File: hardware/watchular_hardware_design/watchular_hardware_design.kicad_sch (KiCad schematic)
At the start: 23 parts, among them Q1 BC817, U1 ESP32-C3FH4, U2 W25Q16JVSSIQ

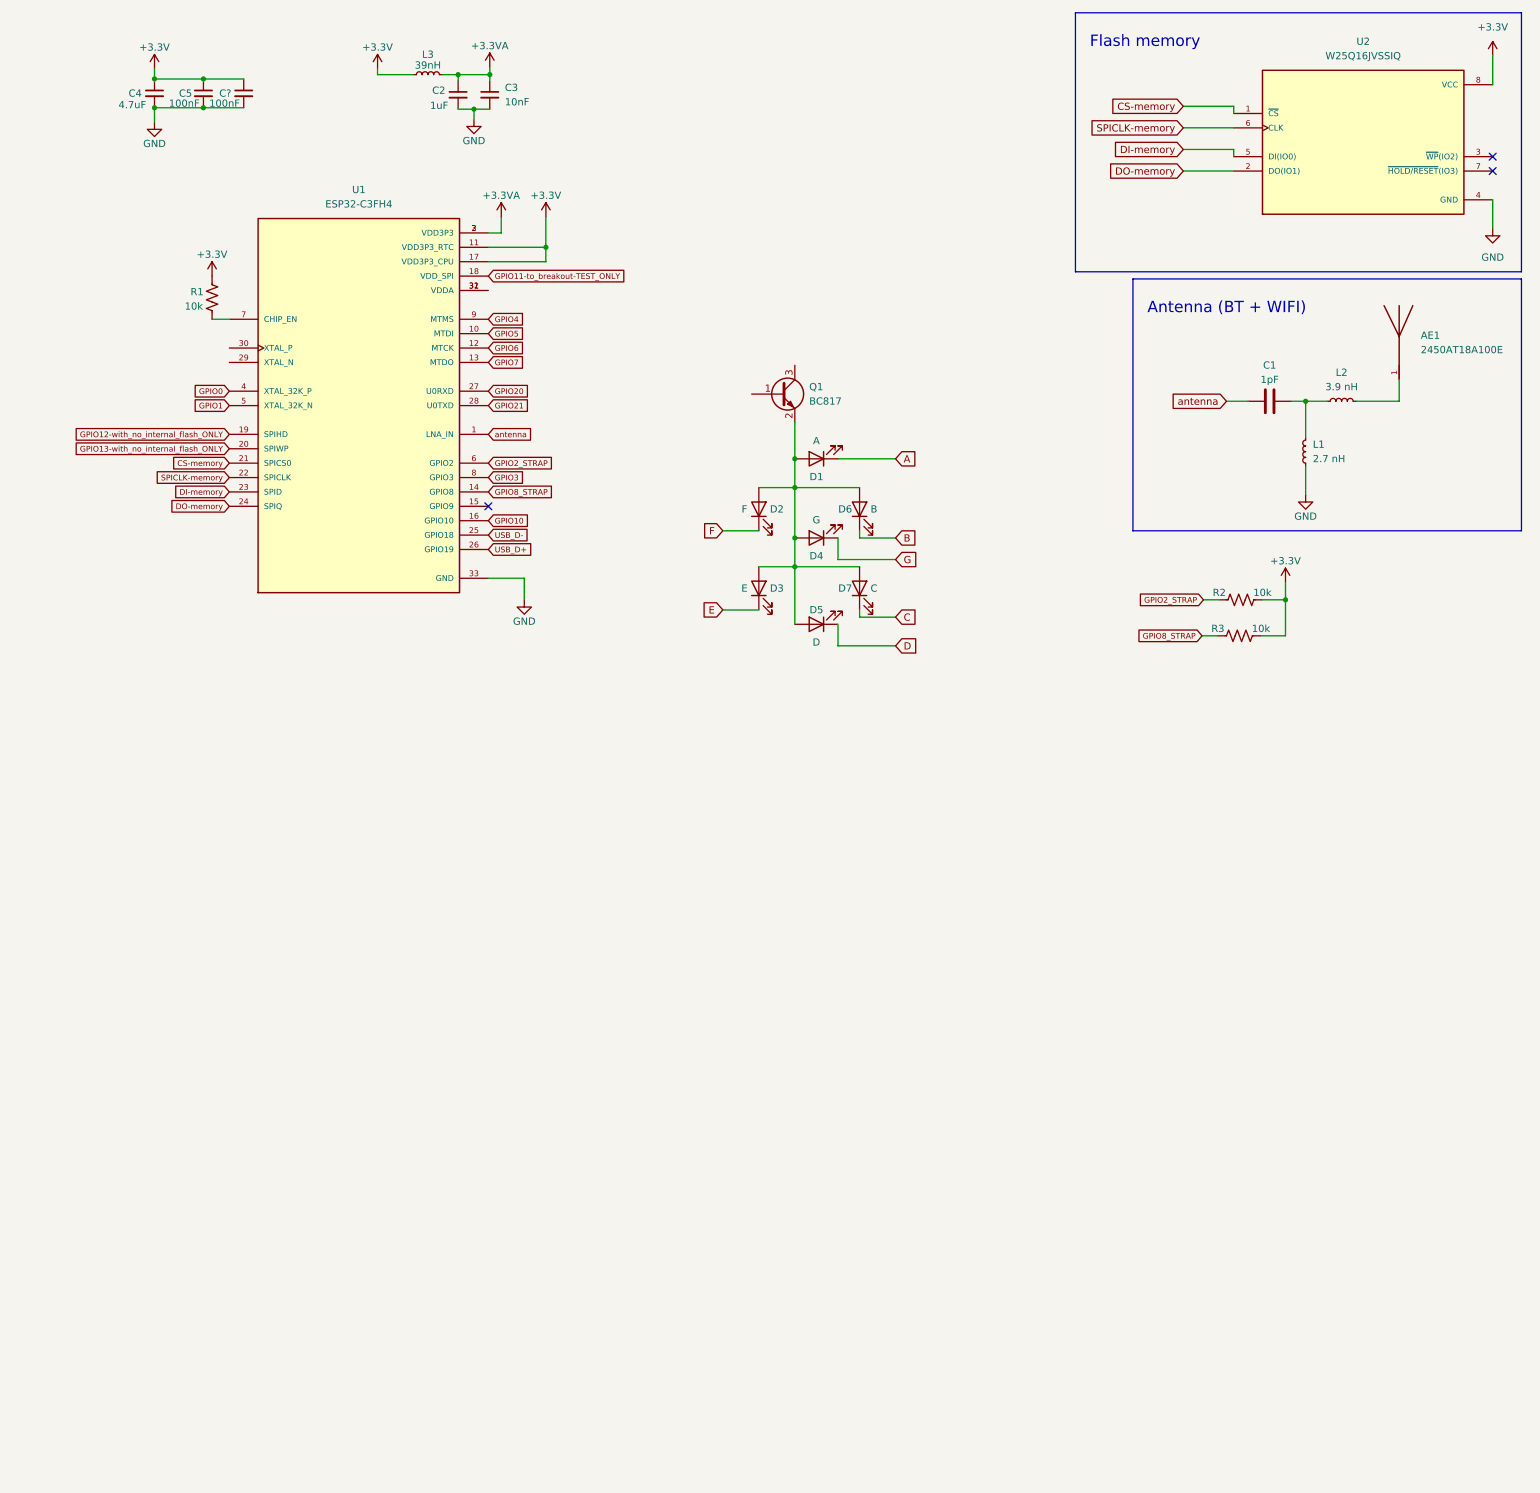
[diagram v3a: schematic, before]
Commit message: Finished the boiler plate for ESP32C3.
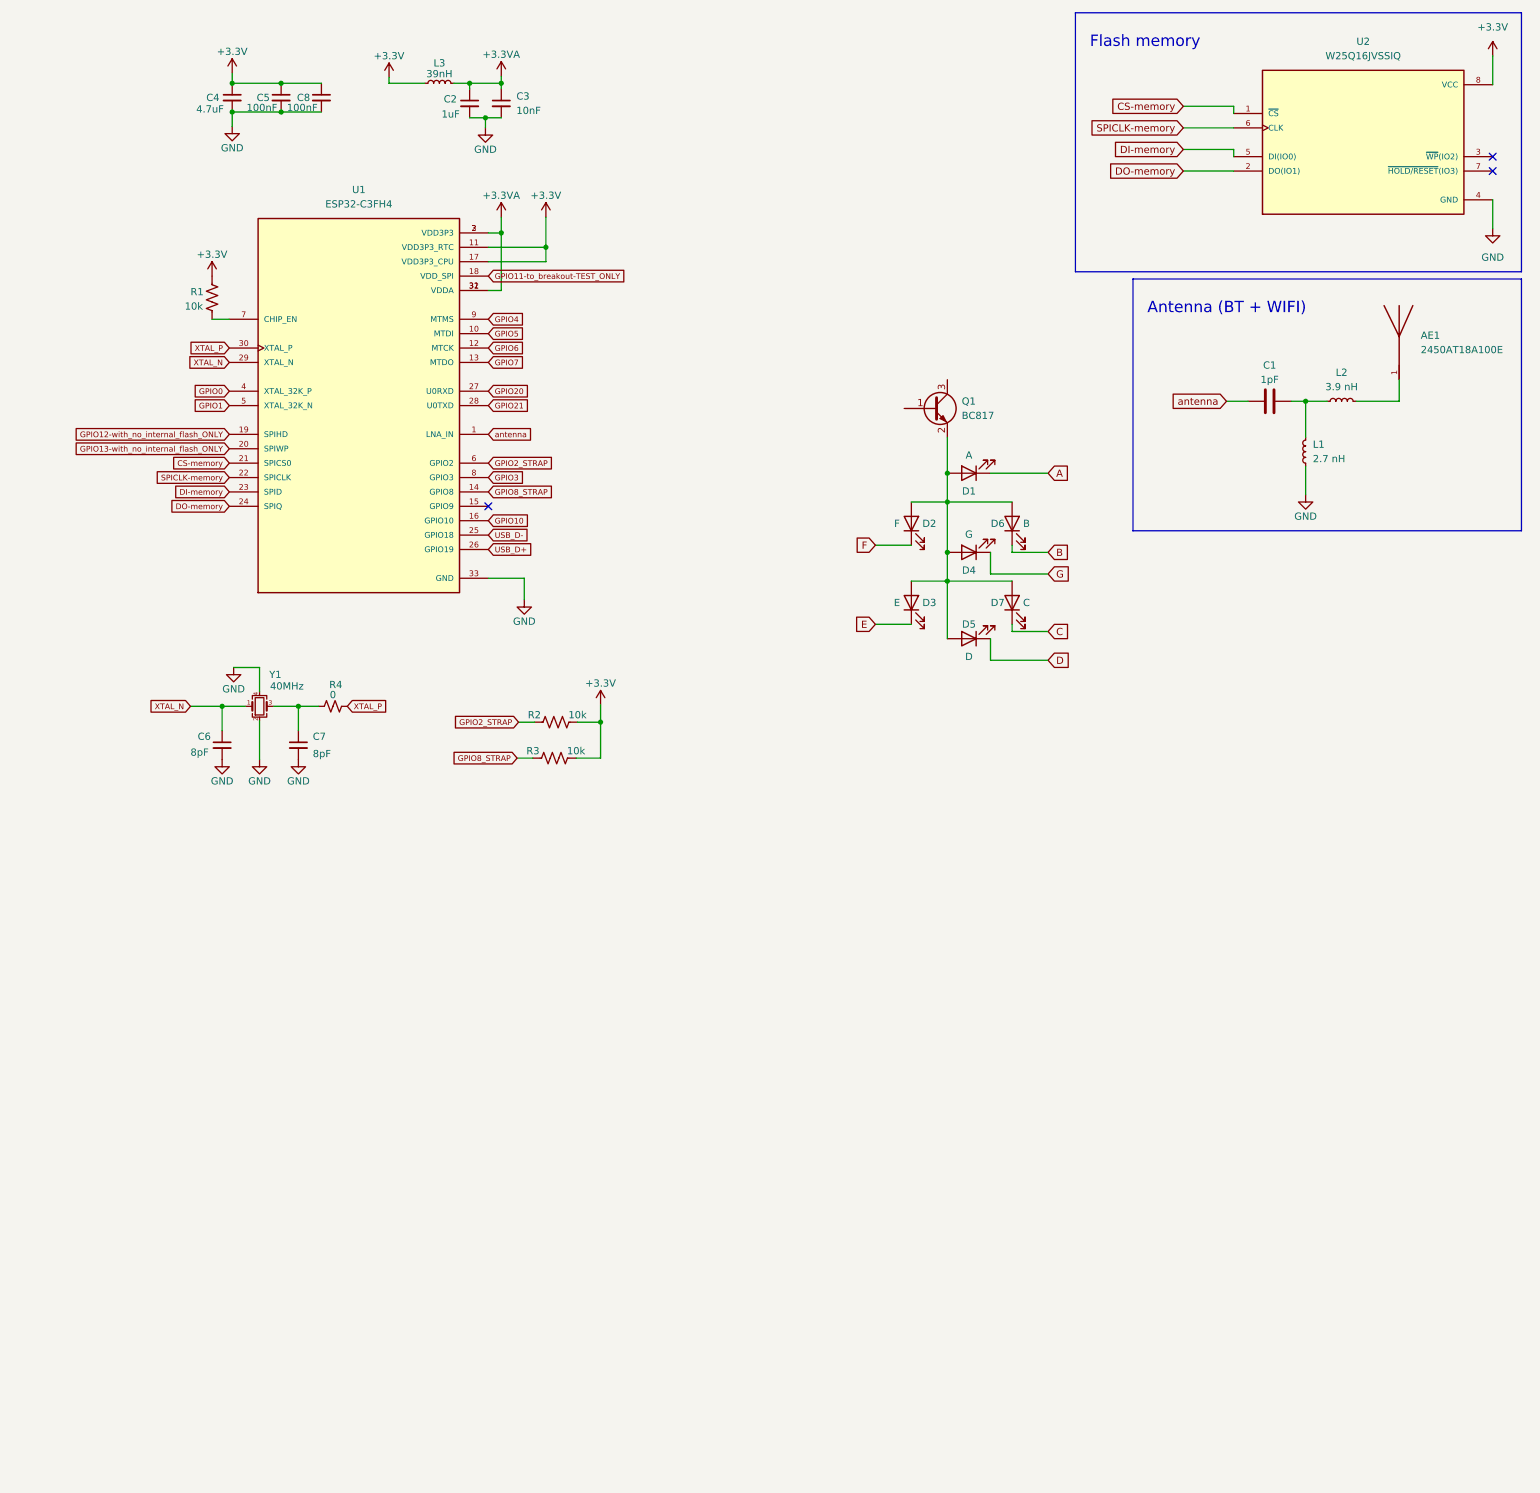
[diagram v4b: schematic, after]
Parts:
- added C6, C7: 8pF, Capacitor_SMD:C_0402_1005Metric_Pad0.74x0.62mm_HandSolder, symbol Device:C_Small
- added R4: 0, Resistor_SMD:R_01005_0402Metric_Pad0.57x0.30mm_HandSolder, symbol Device:R_Small_US
- added Y1: 40MHz, Crystal:Crystal_SMD_2016-4Pin_2.0x1.6mm, symbol Device:Crystal_GND24_Small
- gave numbers to parts that had none: 1
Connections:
- net +3.3VA: now also U1.31 (VDDA), U1.32 (VDDA)
- net GND: now also C6.2, C7.2, Y1.2, Y1.4
- net XTAL_N: now reaches U1.29 (XTAL_N)
- net XTAL_N: now also C6.1, Y1.1
- net XTAL_P: now reaches U1.30 (XTAL_P)
- net XTAL_P: now also R4.2
- new net: C7.1, R4.1, Y1.3
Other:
- moved on the sheet: C2, C3, C4, C5, C8, D1, D2, D3, D4, D5, D6, D7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

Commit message: Clean up the schematic.
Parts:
- removed D1: A, LED_SMD:LED_0603_1608Metric, symbol Device:LED
- removed D2: F, LED_SMD:LED_0603_1608Metric, symbol Device:LED
- removed D3: E, LED_SMD:LED_0603_1608Metric, symbol Device:LED
- removed D4: G, LED_SMD:LED_0603_1608Metric, symbol Device:LED
- removed D5: D, LED_SMD:LED_0603_1608Metric, symbol Device:LED
- removed D6: B, LED_SMD:LED_0603_1608Metric, symbol Device:LED
- removed D7: C, LED_SMD:LED_0603_1608Metric, symbol Device:LED
- removed Q1: BC817, Package_TO_SOT_SMD:SOT-23, symbol Transistor_BJT:BC817
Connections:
- net GPIO9_STRAP: now reaches U1.15 (GPIO9)
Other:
- added sheet peripherals (peripherals.kicad_sch)
- note added: "External clock"
- note added: "MCU ESP32C3 w/o extension --> no internal flash ESP32C3 w/ extension --> has internal flash"
- note added: "Power Filtering"
- note added: "Strap Pins"
- moved on the sheet: AE1, C1, C2, C3, C4, C5, C6, C7, C8, L1, L2, L3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

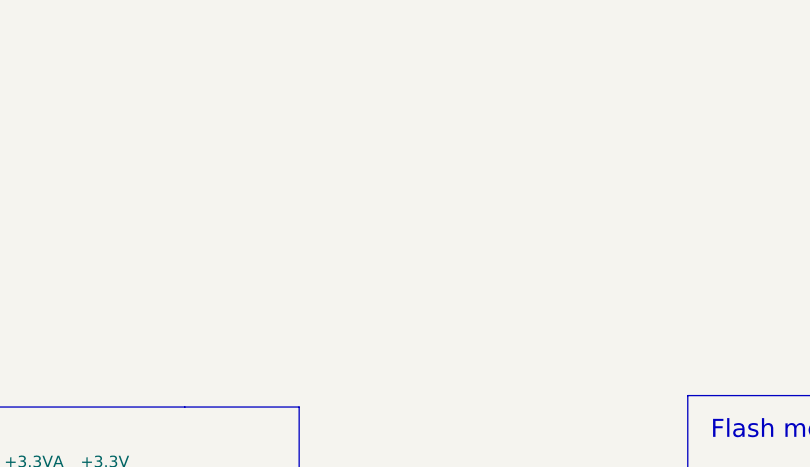
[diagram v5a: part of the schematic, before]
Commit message: Imported the USB-C
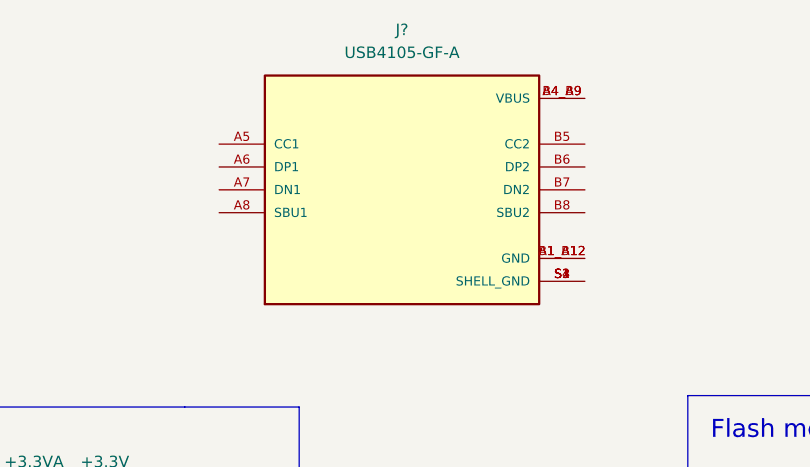
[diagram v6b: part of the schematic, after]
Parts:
- added J?: USB4105-GF-A, USBC-USB4105-GF-A:GCT_USB4105-GF-A, symbol USB4105-GF-A:USB4105-GF-A
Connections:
- new net: J?.A1_B12 (GND), J?.B1_A12 (GND)
- new net: J?.A4_B9 (VBUS), J?.B4_A9 (VBUS)
- new net: J?.S1 (SHELL_GND), J?.S2 (SHELL_GND), J?.S3 (SHELL_GND), J?.S4 (SHELL_GND)
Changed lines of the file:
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@@
     (pin "2")
+  )
+  (symbol (lib_id "USB4105-GF-A:USB4105-GF-A") (at 165.1 35.56 0) (unit 1)
+    (in_bom yes) (on_board yes) (fields_autoplaced)
+    (property "Reference" "J?" (id 0) (at 165.1 17.78 0))
+    (property "Value" "USB4105-GF-A" (id 1) (at 165.1 20.32 0))
+    (property "Footprint" "USBC-USB4105-GF-A:GCT_USB4105-GF-A" (id 2) (at 165.1 35.56 0)
+      (effects (font (size 1.27 1.27)) (justify left bottom) hide)
+    )
+    (property "Datasheet" "" (id 3) (at 165.1 35.56 0)
+      (effects (font (size 1.27 1.27)) (justify left bottom) hide)
+    )
+    (property "MANUFACTURER" "GCT" (id 4) (at 165.1 35.56 0)
+      (effects (font (size 1.27 1.27)) (justify left bottom) hide)
+    )
+    (property "PARTREV" "A3" (id 5) (at 165.1 35.56 0)
+      (effects (font (size 1.27 1.27)) (justify left bottom) hide)
+    )
+    (property "MAXIMUM_PACKAGE_HEIGHT" "3.31 mm" (id 6) (at 165.1 35.56 0)
+      (effects (font (size 1.27 1.27)) (justify left bottom) hide)
+    )
+    (property "STANDARD" "Manufacturer Recommendations" (id 7) (at 165.1 35.56 0)
+      (effects (font (size 1.27 1.27)) (justify left bottom) hide)
+    )
+    (pin "A1_B12")
+    (pin "A4_B9")
+    (pin "A5")
+    (pin "A6")
+    (pin "A7")
+    (pin "A8")
+    (pin "B1_A12")
+    (pin "B4_A9")
+    (pin "B5")
+    (pin "B6")
+    (pin "B7")
+    (pin "B8")
+    (pin "S1")
+    (pin "S2")
+    (pin "S3")
+    (pin "S4")
   )
   (symbol (lib_id "Device:R_US") (at 73.152 83.82 0) (unit 1)
@@
       (reference "D7") (unit 1) (value "C") (footprint "LED_SMD:LED_0603_1608Metric")
     )
+    (path "/e10a3c85-8073-4ae2-ab18-9aae4c5ce096"
+      (reference "J?") (unit 1) (value "USB4105-GF-A") (footprint "USBC-USB4105-GF-A:GCT_USB4105-GF-A")
+    )
     (path "/1f1de665-878b-408f-bbe7-a6c746e0bfb6"
